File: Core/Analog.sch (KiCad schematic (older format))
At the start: 43 parts, among them J10 AudioJack3_SwitchTR, J7 AudioJack3_SwitchTR, J8 AudioJack3_SwitchTR, J9 AudioJack3_SwitchTR, U4 TL072, U6 ES9023P, U7 PCM1808, U8 TL072

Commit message: Fix symbols
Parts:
- U6: symbol Custom:ES9023P -> CustomLib:ES9023P
- U7: symbol Custom:PCM1808 -> CustomLib:PCM1808
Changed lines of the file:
@@
 $EndDescr
 $Comp
-L Custom:PCM1808 U?
+L CustomLib:PCM1808 U?
 U 1 1 60A61853
 P 5550 2750
@@
 	9500 1100 9900 1100
 $Comp
-L Custom:ES9023P U6
+L CustomLib:ES9023P U6
 U 1 1 609A13DB
 P 3500 5900

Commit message: Include symbol library
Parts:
- U6: symbol CustomLib:ES9023P -> Custom_Sym:ES9023P
- U7: symbol CustomLib:PCM1808 -> Custom_Sym:PCM1808
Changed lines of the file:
@@
 $EndDescr
 $Comp
-L CustomLib:PCM1808 U?
+L Custom_Sym:PCM1808 U?
 U 1 1 60A61853
 P 5550 2750
@@
 	9500 1100 9900 1100
 $Comp
-L CustomLib:ES9023P U6
+L Custom_Sym:ES9023P U6
 U 1 1 609A13DB
 P 3500 5900

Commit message: Add custom footprints
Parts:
- J10, J7, J8, J9: footprint CustomLib:STX3100_Angled_3.5mm -> Custom_FP:STX3100_Angled_3.5mm
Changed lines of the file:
@@
 F 0 "J9" H 9820 725 50  0000 R CNN
 F 1 "AudioJack3_SwitchTR" H 9820 634 50  0000 R CNN
-F 2 "CustomLib:STX3100_Angled_3.5mm" H 10100 800 50  0001 C CNN
+F 2 "Custom_FP:STX3100_Angled_3.5mm" H 10100 800 50  0001 C CNN
 F 3 "~" H 10100 800 50  0001 C CNN
 	1    10100 800
@@
 F 0 "J10" H 9820 1875 50  0000 R CNN
 F 1 "AudioJack3_SwitchTR" H 9820 1784 50  0000 R CNN
-F 2 "CustomLib:STX3100_Angled_3.5mm" H 10100 1950 50  0001 C CNN
+F 2 "Custom_FP:STX3100_Angled_3.5mm" H 10100 1950 50  0001 C CNN
 F 3 "~" H 10100 1950 50  0001 C CNN
 	1    10100 1950
@@
 F 0 "J8" H 7920 5625 50  0000 R CNN
 F 1 "AudioJack3_SwitchTR" H 7920 5534 50  0000 R CNN
-F 2 "CustomLib:STX3100_Angled_3.5mm" H 8200 5700 50  0001 C CNN
+F 2 "Custom_FP:STX3100_Angled_3.5mm" H 8200 5700 50  0001 C CNN
 F 3 "~" H 8200 5700 50  0001 C CNN
 	1    8200 5700
@@
 F 0 "J7" H 7920 4825 50  0000 R CNN
 F 1 "AudioJack3_SwitchTR" H 7920 4734 50  0000 R CNN
-F 2 "CustomLib:STX3100_Angled_3.5mm" H 8200 4900 50  0001 C CNN
+F 2 "Custom_FP:STX3100_Angled_3.5mm" H 8200 4900 50  0001 C CNN
 F 3 "~" H 8200 4900 50  0001 C CNN
 	1    8200 4900

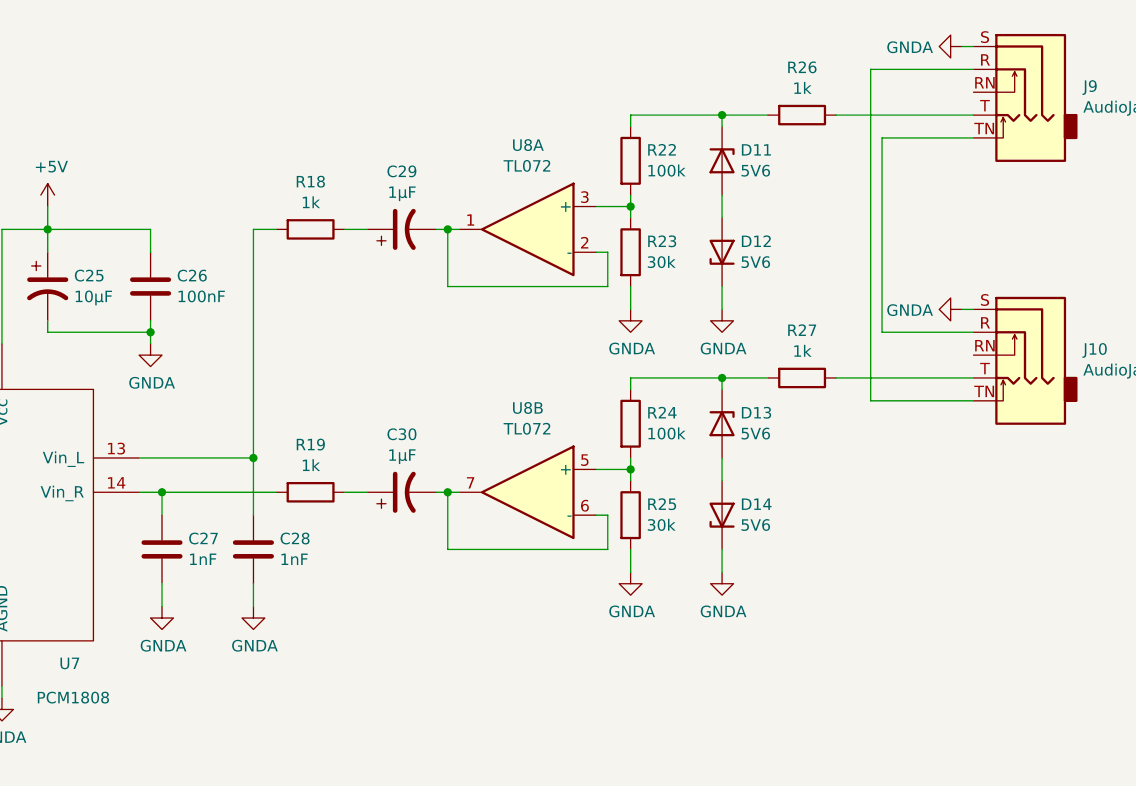
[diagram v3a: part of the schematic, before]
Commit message: Reduce distortion in ADC circuit
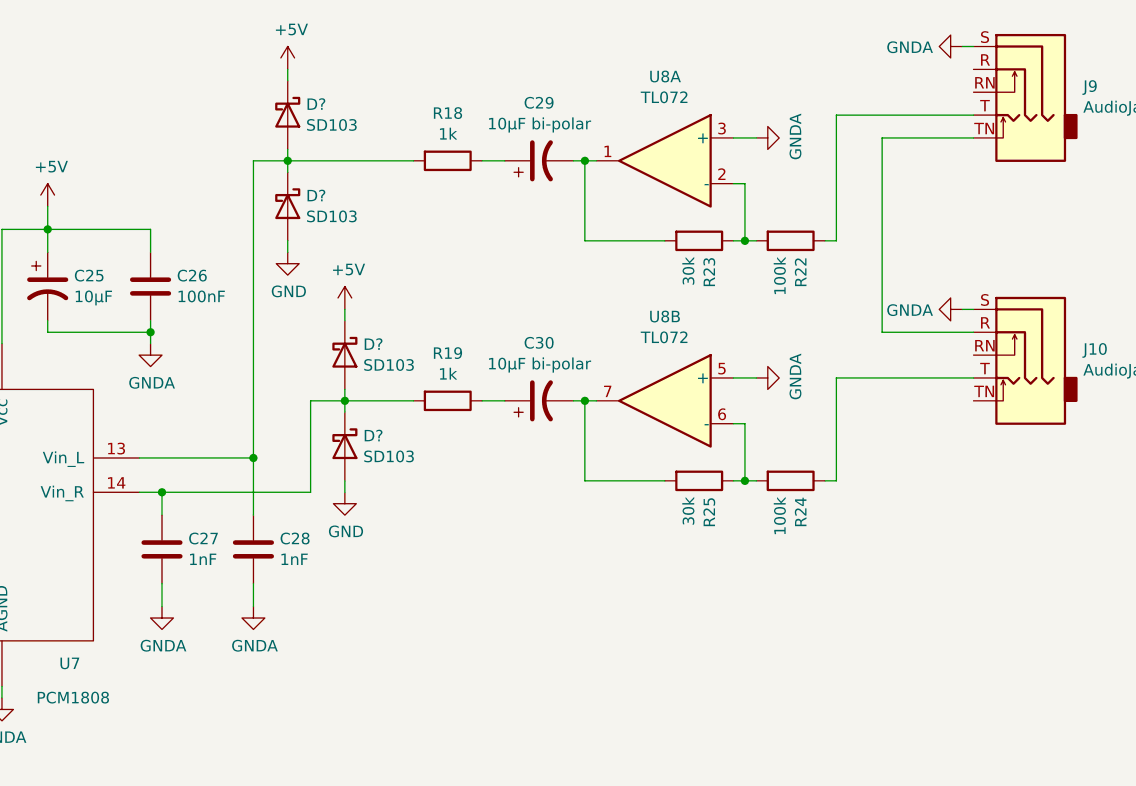
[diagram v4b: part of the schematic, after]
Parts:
- removed D11, D12, D13, D14: 5V6, Diode_SMD:D_SOD-123, symbol Device:D_Zener
- removed R26, R27: 1k, Resistor_SMD:R_0603_1608Metric, symbol Device:R
- added D? (x4): SD103, Diode_SMD:D_SOD-323_HandSoldering, symbol Device:D_Schottky
- C29, C30: value 1µF -> 10µF bi-polar; footprint Capacitor_SMD:CP_Elec_4x5.4 -> Capacitor_SMD:CP_Elec_5x5.8
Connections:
- net +5V: now also D?.1 (K), D?.1 (K)
- net GND: now also D?.2 (A), D?.2 (A)
- net GNDA: now also U8.3 (+), U8.5 (+); no longer R23.2, R25.2
- net at C28.1, R18.2, U7.13 (Vin_L): now also D?.1 (K), D?.2 (A)
- net at C27.1, R19.2, U7.14 (Vin_R): now also D?.1 (K), D?.2 (A)
- net at C29.2, U8.1: now also R23.2; no longer U8.2 (-)
- net at C30.2, U8.7: now also R25.2; no longer U8.6 (-)
- net at R22.2, R23.1: now also U8.2 (-); no longer U8.3 (+)
- net at R22.1: now also J9.T
- net at R24.2, R25.1: now also U8.6 (-); no longer U8.5 (+)
- net at R24.1: now also J10.T
- net at J9.R: no longer J10.TN
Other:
- moved on the sheet: C29, C30, R18, R19, R22, R23, R24, R25, U8A, U8B

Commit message: Add IO and bootloader buttons
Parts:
- gave numbers to parts that had none: 4
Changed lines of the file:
@@
 P 7150 2450
 AR Path="/6095E754/62C702AD" Ref="D?"  Part="1"
-AR Path="/60A3EECB/62C702AD" Ref="D?"  Part="1"
-F 0 "D?" V 7104 2530 50  0000 L CNN
+AR Path="/60A3EECB/62C702AD" Ref="D12"  Part="1"
+F 0 "D12" V 7104 2530 50  0000 L CNN
 F 1 "SD103" V 7195 2530 50  0000 L CNN
 F 2 "Diode_SMD:D_SOD-323_HandSoldering" H 7150 2450 50  0001 C CNN
@@
 P 7150 2050
 AR Path="/6095E754/62C76156" Ref="D?"  Part="1"
-AR Path="/60A3EECB/62C76156" Ref="D?"  Part="1"
-F 0 "D?" V 7104 2130 50  0000 L CNN
+AR Path="/60A3EECB/62C76156" Ref="D11"  Part="1"
+F 0 "D11" V 7104 2130 50  0000 L CNN
 F 1 "SD103" V 7195 2130 50  0000 L CNN
 F 2 "Diode_SMD:D_SOD-323_HandSoldering" H 7150 2050 50  0001 C CNN
@@
 P 6900 1000
 AR Path="/6095E754/62C90F6D" Ref="D?"  Part="1"
-AR Path="/60A3EECB/62C90F6D" Ref="D?"  Part="1"
-F 0 "D?" V 6854 1080 50  0000 L CNN
+AR Path="/60A3EECB/62C90F6D" Ref="D3"  Part="1"
+F 0 "D3" V 6854 1080 50  0000 L CNN
 F 1 "SD103" V 6945 1080 50  0000 L CNN
 F 2 "Diode_SMD:D_SOD-323_HandSoldering" H 6900 1000 50  0001 C CNN
@@
 P 6900 1400
 AR Path="/6095E754/62BE2C95" Ref="D?"  Part="1"
-AR Path="/60A3EECB/62BE2C95" Ref="D?"  Part="1"
-F 0 "D?" V 6854 1480 50  0000 L CNN
+AR Path="/60A3EECB/62BE2C95" Ref="D4"  Part="1"
+F 0 "D4" V 6854 1480 50  0000 L CNN
 F 1 "SD103" V 6945 1480 50  0000 L CNN
 F 2 "Diode_SMD:D_SOD-323_HandSoldering" H 6900 1400 50  0001 C CNN
@@
 	7150 2300 7150 2250
 $Comp
-L power:GND #PWR?
+L power:GND #PWR0202
 U 1 1 62CBDED9
 P 6900 1600
-F 0 "#PWR?" H 6900 1350 50  0001 C CNN
+F 0 "#PWR0202" H 6900 1350 50  0001 C CNN
 F 1 "GND" H 6905 1427 50  0000 C CNN
 F 2 "" H 6900 1600 50  0001 C CNN
@@
 $EndComp
 $Comp
-L power:GND #PWR?
+L power:GND #PWR0203
 U 1 1 62CBED8A
 P 7150 2650
-F 0 "#PWR?" H 7150 2400 50  0001 C CNN
+F 0 "#PWR0203" H 7150 2400 50  0001 C CNN
 F 1 "GND" H 7155 2477 50  0000 C CNN
 F 2 "" H 7150 2650 50  0001 C CNN
@@
 	6900 1200 7450 1200
 $Comp
-L power:+5V #PWR?
+L power:+5V #PWR0204
 U 1 1 62CCAA9C
 P 6900 800
-F 0 "#PWR?" H 6900 650 50  0001 C CNN
+F 0 "#PWR0204" H 6900 650 50  0001 C CNN
 F 1 "+5V" H 6915 973 50  0000 C CNN
 F 2 "" H 6900 800 50  0001 C CNN
@@
 $EndComp
 $Comp
-L power:+5V #PWR?
+L power:+5V #PWR0205
 U 1 1 62CCBB9D
 P 7150 1850
-F 0 "#PWR?" H 7150 1700 50  0001 C CNN
+F 0 "#PWR0205" H 7150 1700 50  0001 C CNN
 F 1 "+5V" H 7165 2023 50  0000 C CNN
 F 2 "" H 7150 1850 50  0001 C CNN

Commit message: Fix DAC amplitude
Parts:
- R16, R17: value 42k -> 27k
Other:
- note added: "1.9Vpp RMS?? => 2.7Vpp"
- note removed: "1.9Vpp"
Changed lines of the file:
@@
 	2850 6150 2950 6150
 Text Notes 4150 5400 0    50   ~ 0
-1.9Vpp
+1.9Vpp RMS?? => 2.7Vpp
 Text GLabel 2850 5500 0    50   Input ~ 0
 I2S_SCK
@@
 P 6950 5450
 F 0 "R16" V 6743 5450 50  0000 C CNN
-F 1 "42k" V 6834 5450 50  0000 C CNN
+F 1 "27k" V 6834 5450 50  0000 C CNN
 F 2 "Resistor_SMD:R_0603_1608Metric" V 6880 5450 50  0001 C CNN
 F 3 "~" H 6950 5450 50  0001 C CNN
@@
 P 6950 6250
 F 0 "R17" V 6743 6250 50  0000 C CNN
-F 1 "42k" V 6834 6250 50  0000 C CNN
+F 1 "27k" V 6834 6250 50  0000 C CNN
 F 2 "Resistor_SMD:R_0603_1608Metric" V 6880 6250 50  0001 C CNN
 F 3 "~" H 6950 6250 50  0001 C CNN
